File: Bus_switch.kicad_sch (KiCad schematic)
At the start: 8 parts, among them J3 Conn_01x04_Pin, U1 SN74CB3Q3384APW

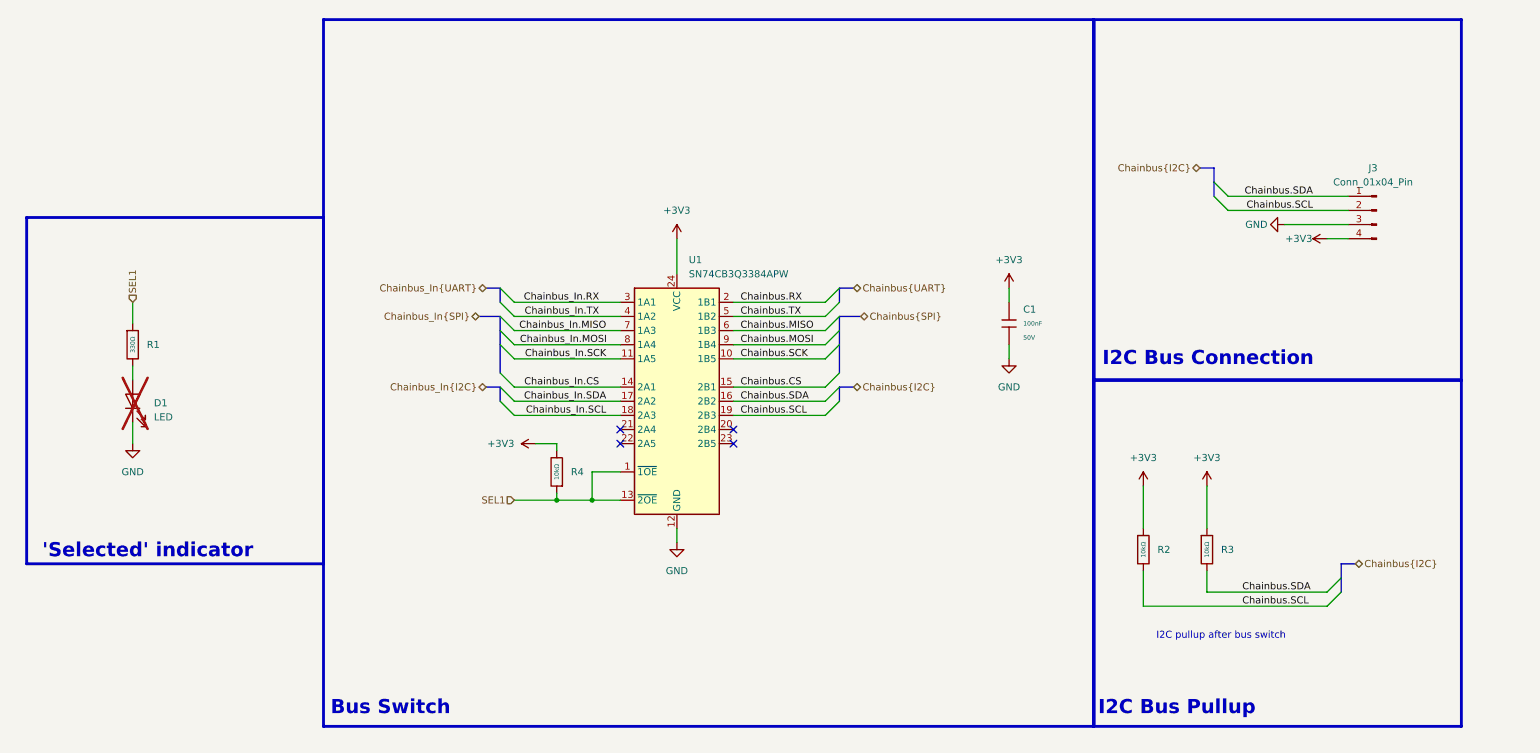
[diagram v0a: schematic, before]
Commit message: updated Bus switch to one stocked by TME
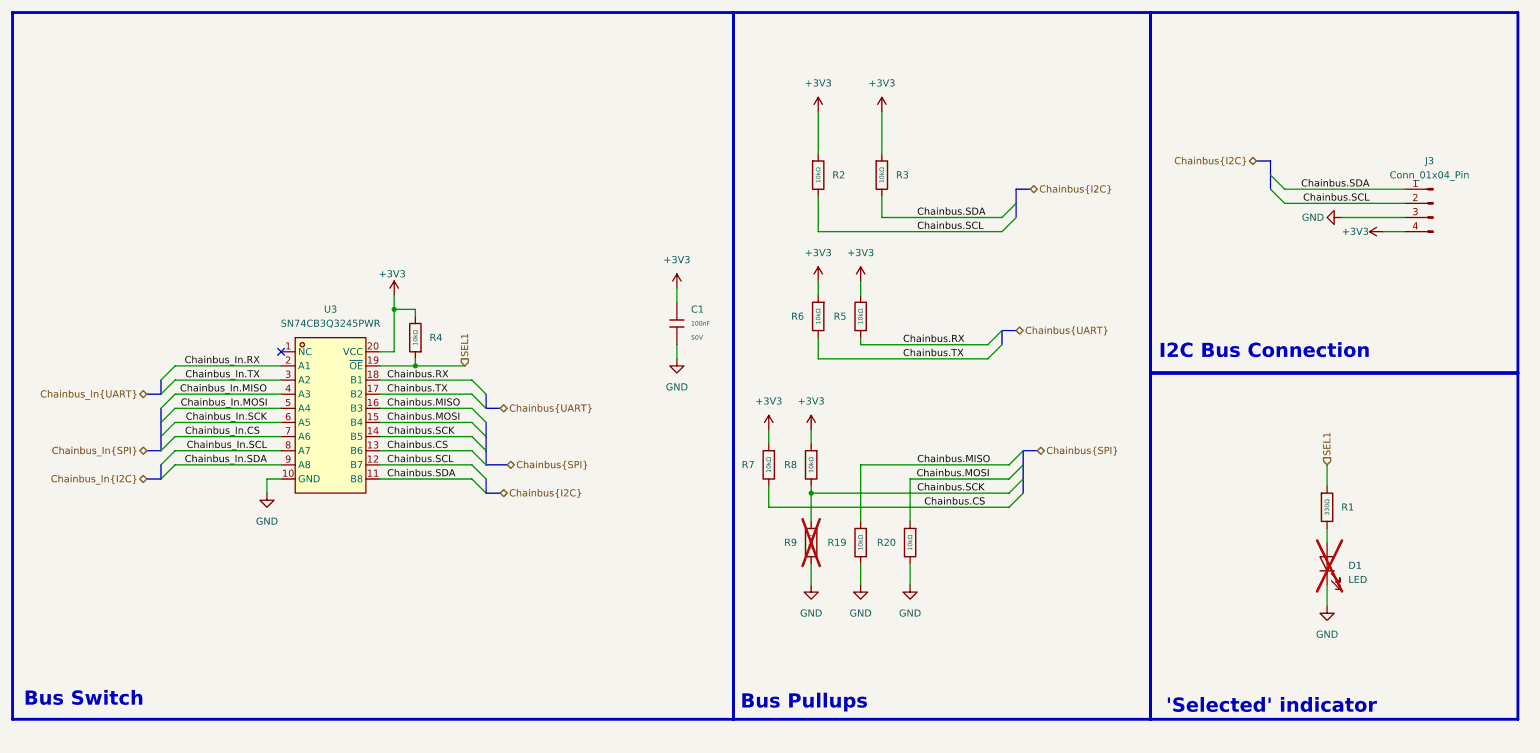
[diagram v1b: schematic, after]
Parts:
- removed U1: SN74CB3Q3384APW, Package_SO:TSSOP-24_4.4x7.8mm_P0.65mm, symbol 74xx:SN74CB3Q3384APW
- added R19, R20, R5, R6, R7, R8, R9: 10kΩ, PCM_JLCPCB:R_0402, symbol PCM_JLCPCB-Resistors:0402,10kΩ
- added U3: SN74CB3Q3245PWR, SN74CB3Q3245PWR:TSSOP-20_L6.5-W4.4-P0.65-LS6.4-BL, symbol SN74CB3Q3245PWR:SN74CB3Q3245PWR
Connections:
- net +3V3: now also R5.1, R6.1, R7.1, R8.1, U3.20 (VCC)
- net Chainbus.CS: now also R7.2, U3.13 (B6)
- net Chainbus.MISO: now also R19.1, U3.16 (B3)
- net Chainbus.MOSI: now also R20.1, U3.15 (B4)
- net Chainbus.RX: now also R5.2, U3.18 (B1)
- net Chainbus.SCK: now also R8.2, R9.1, U3.14 (B5)
- net Chainbus.SCL: now also U3.12 (B7)
- net Chainbus.SDA: now also U3.11 (B8)
- net Chainbus.TX: now also R6.2, U3.17 (B2)
- net Chainbus_In.CS: now also U3.7 (A6)
- net Chainbus_In.MISO: now also U3.4 (A3)
- net Chainbus_In.MOSI: now also U3.5 (A4)
- net Chainbus_In.RX: now also U3.2 (A1)
- net Chainbus_In.SCK: now also U3.6 (A5)
- net Chainbus_In.SCL: now also U3.8 (A7)
- net Chainbus_In.SDA: now also U3.9 (A8)
- net Chainbus_In.TX: now also U3.3 (A2)
- net GND: now also R19.2, R20.2, R9.2, U3.10 (GND)
- net SEL1: now also U3.19 (~{OE})
- no-connect marks 4 -> 1
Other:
- note added: "Bus Pullups"
- note removed: "I2C Bus Pullup"
- note removed: "I2C pullup after bus switch"
- moved on the sheet: C1, D1, J3, R1, R2, R3, R4

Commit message: polished the schemtic
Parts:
- removed D1: LED, LED_SMD:LED_0603_1608Metric, symbol Device:LED
- removed R4: 10kΩ, PCM_JLCPCB:R_0402, symbol PCM_JLCPCB-Resistors:0402,10kΩ
- added D5: Red, PCM_JLCPCB:D_0603, symbol PCM_JLCPCB-Diodes:LED,0603,Red
- added R21: 10kΩ, PCM_JLCPCB:R_0402, symbol PCM_JLCPCB-Resistors:0402,10kΩ
- R5: now not fitted; now left out of the parts list
- R9: now fitted; now in the parts list
- U3: TME (none) -> SN74CB3Q3245PWR
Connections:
- net +3V3: now also R19.1, D5.2, R21.2; no longer R5.1
- net Chainbus.CS: now also R2.2; no longer R7.2
- net Chainbus.MISO: now also R9.1; no longer R19.1
- net Chainbus.RX: now also R8.2; no longer R5.2
- net Chainbus.SCK: now also R3.2, R5.1; no longer R8.2, R9.1
- net Chainbus.SCL: now also R6.2; no longer R2.2
- net Chainbus.SDA: now also R19.2; no longer R3.2
- net Chainbus.TX: now also R7.2; no longer R6.2
- net GND: now also R5.2; no longer R19.2
- net SEL1: now also R21.1
- net at R1.2: now also D5.1

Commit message: PCB design
In progress
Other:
- title: MMS3 Hat template small (Change Me) -> MMS3 Hat servo controller
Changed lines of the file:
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@@
 	(paper "A4")
 	(title_block
-		(title "MMS3 Hat template small (Change Me)")
+		(title "MMS3 Hat servo controller")
 		(date "2026-02-25")
 		(rev "A")
